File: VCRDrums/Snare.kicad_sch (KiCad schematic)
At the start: 90 parts, among them Q501 BC847, Q502 BC857, Q503 BC847, Q504 BC847, Q505 BC847, Q506 BC857, Q507 BC857, U501 TL074, U502 LM13700, U503 TL074

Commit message: clave in kicad
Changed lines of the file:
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@@
 					(size 1.27 1.27)
 				)
+				(hide yes)
 			)
 		)

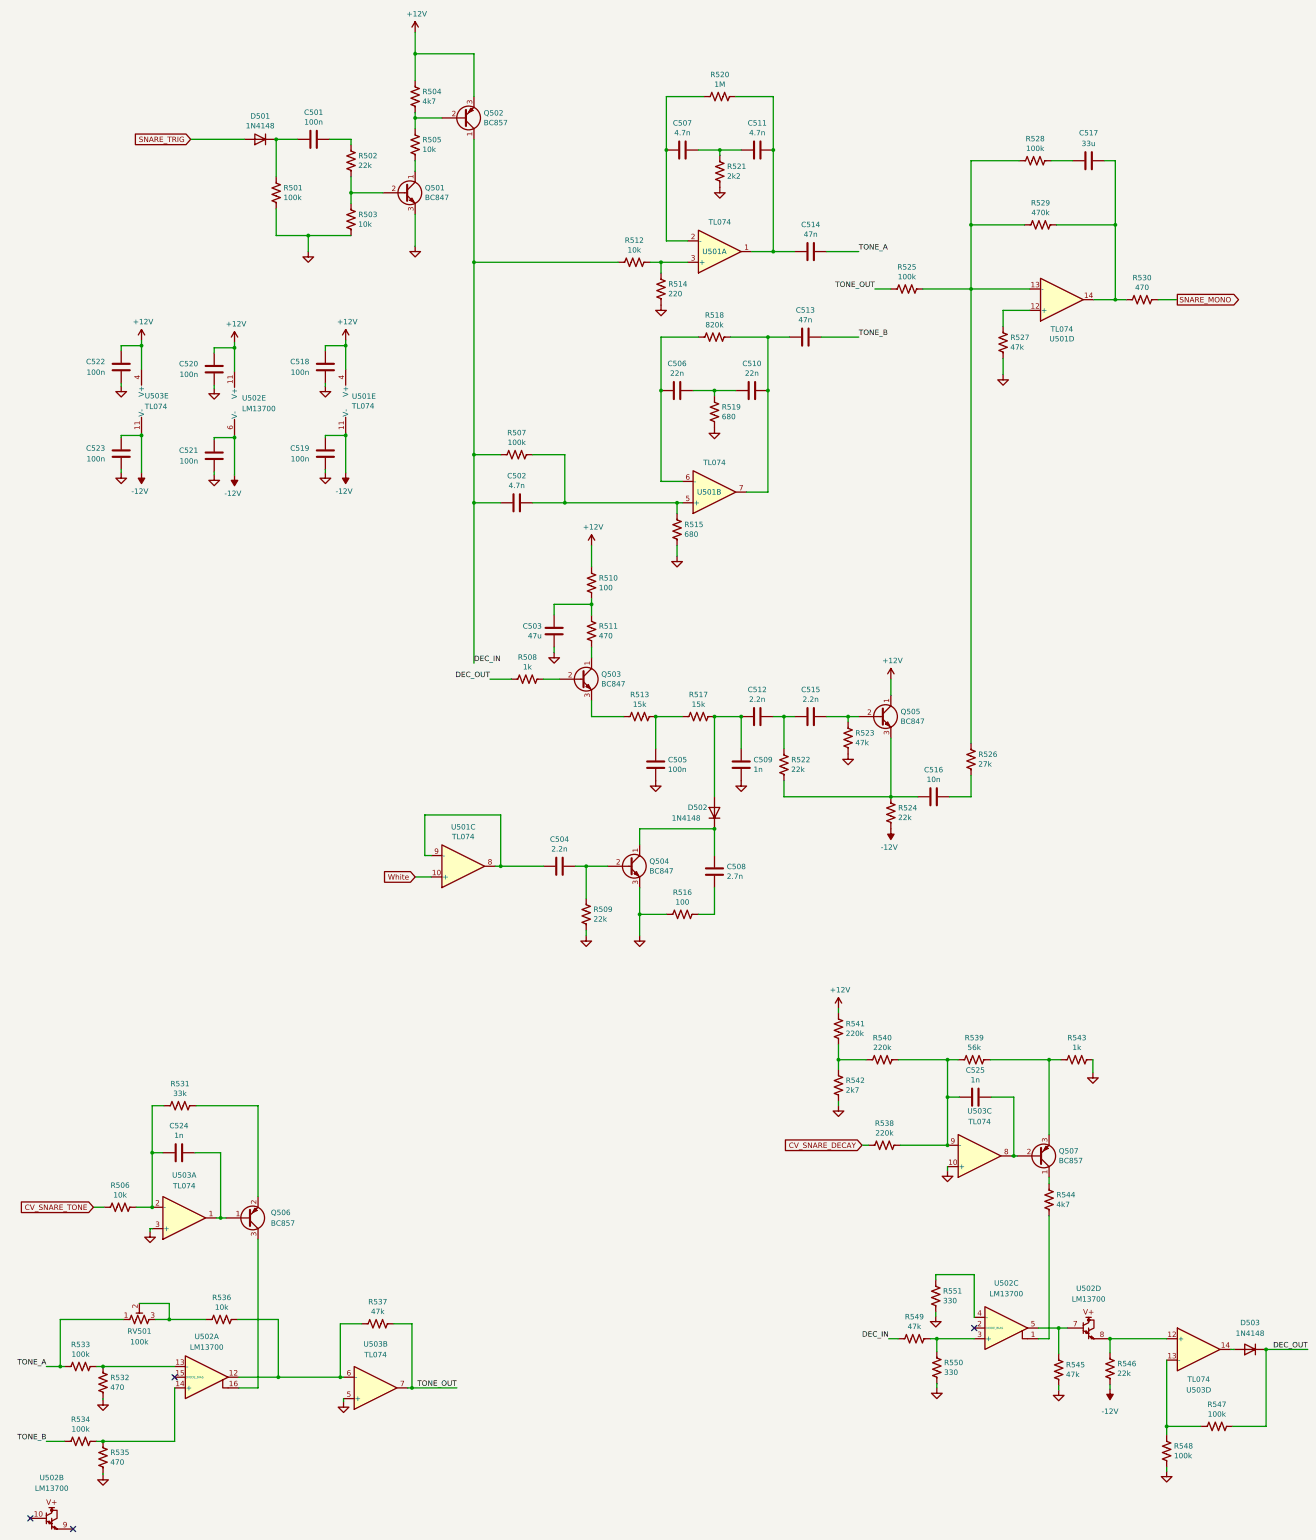
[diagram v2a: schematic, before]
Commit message: mcu skeleton
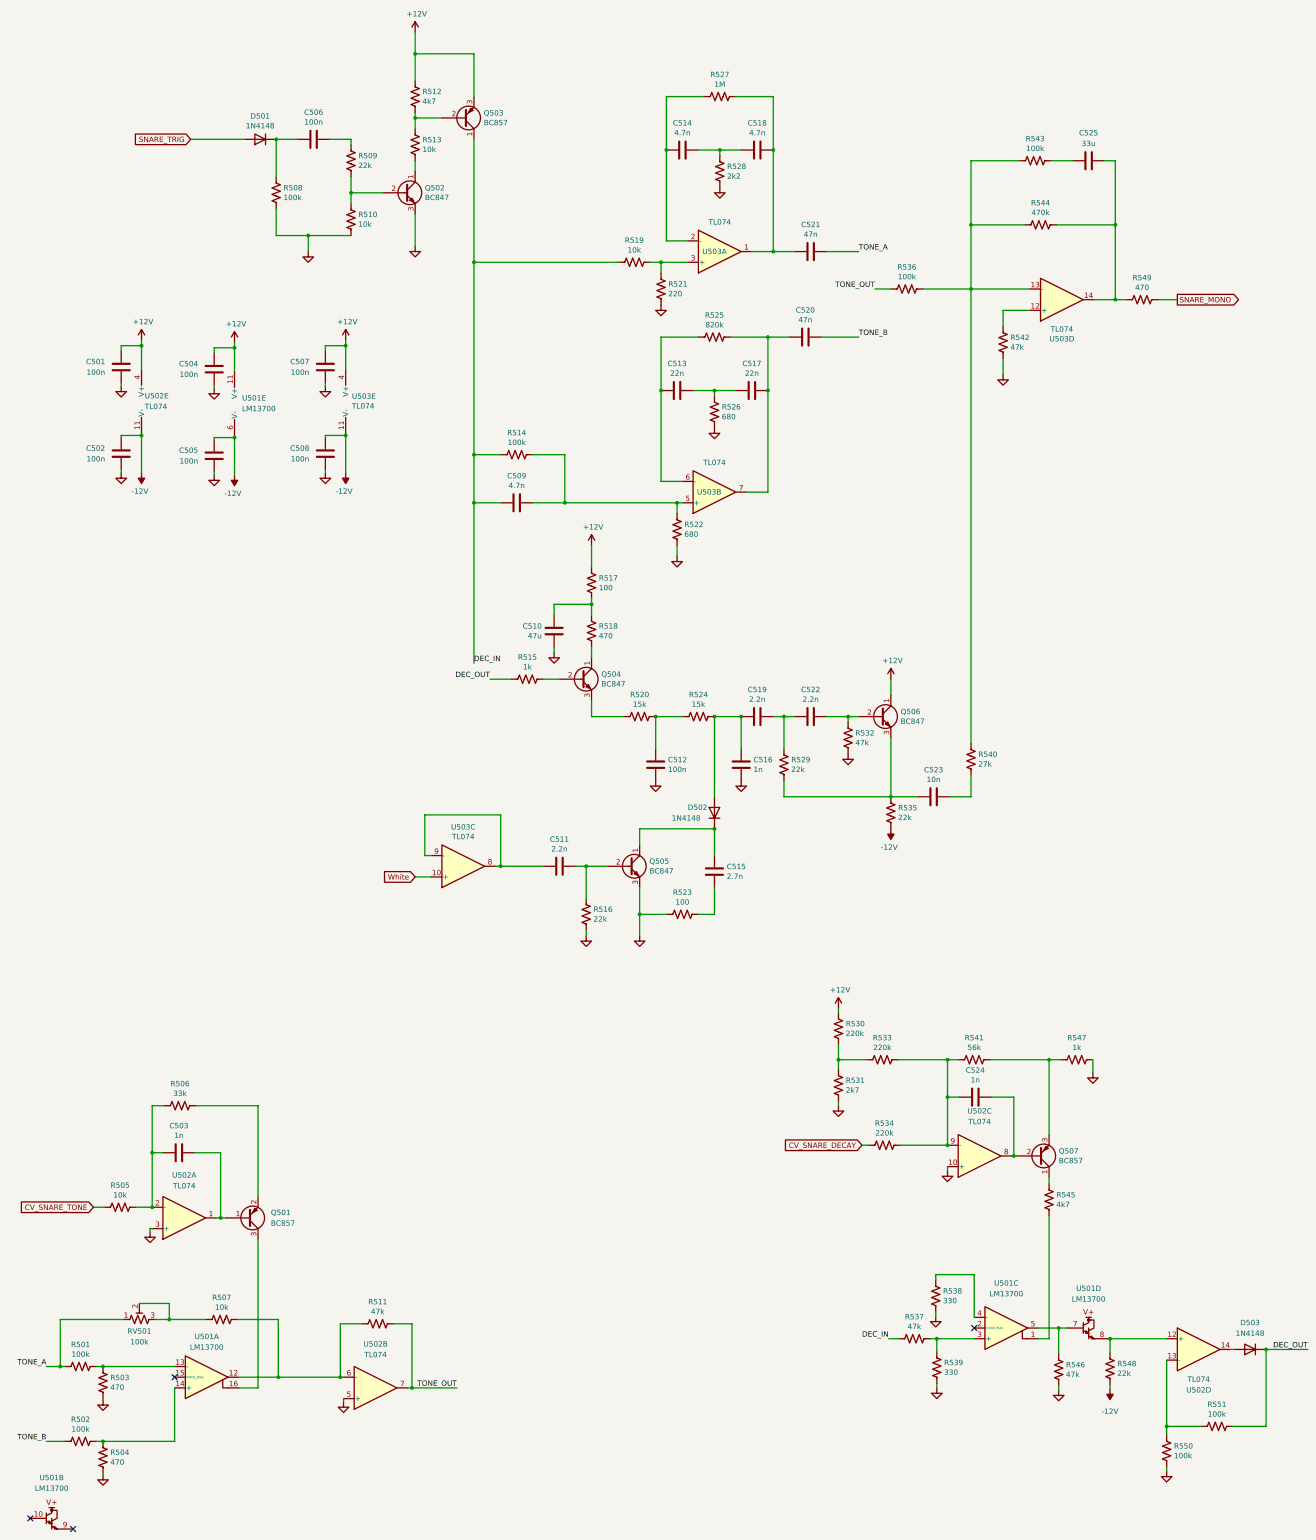
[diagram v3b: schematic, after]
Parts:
- C501: renamed from C522; footprint (none) -> Capacitor_SMD:C_0805_2012Metric
- C502: renamed from C523; footprint (none) -> Capacitor_SMD:C_0805_2012Metric
- C504: renamed from C520; footprint (none) -> Capacitor_SMD:C_0805_2012Metric
- C505: renamed from C521; footprint (none) -> Capacitor_SMD:C_0805_2012Metric
- C507: renamed from C518; footprint (none) -> Capacitor_SMD:C_0805_2012Metric
- C508: renamed from C519; footprint (none) -> Capacitor_SMD:C_0805_2012Metric
- C525: renamed from C517; footprint (none) -> Capacitor_SMD:C_0805_2012Metric
- Q502: renamed from Q501; footprint PCM_4ms_Package_SOT:SOT-23 -> Package_TO_SOT_SMD:SOT-23
- Q503: renamed from Q502; footprint PCM_4ms_Package_SOT:SOT-23 -> Package_TO_SOT_SMD:SOT-23
- Q504: renamed from Q503; footprint PCM_4ms_Package_SOT:SOT-23 -> Package_TO_SOT_SMD:SOT-23
- Q505: renamed from Q504; footprint PCM_4ms_Package_SOT:SOT-23 -> Package_TO_SOT_SMD:SOT-23
- Q506: renamed from Q505; footprint PCM_4ms_Package_SOT:SOT-23 -> Package_TO_SOT_SMD:SOT-23
- Q507: footprint PCM_4ms_Package_SOT:SOT-23 -> Package_TO_SOT_SMD:SOT-23
- R501: renamed from R533; footprint PCM_Resistor_SMD_AKL:R_0805_2012Metric -> Resistor_SMD:R_0805_2012Metric
- R502: renamed from R534; footprint PCM_Resistor_SMD_AKL:R_0805_2012Metric -> Resistor_SMD:R_0805_2012Metric
- R503: renamed from R532; footprint PCM_Resistor_SMD_AKL:R_0805_2012Metric -> Resistor_SMD:R_0805_2012Metric
- R504: renamed from R535; footprint PCM_Resistor_SMD_AKL:R_0805_2012Metric -> Resistor_SMD:R_0805_2012Metric
- R505: renamed from R506; footprint PCM_Resistor_SMD_AKL:R_0805_2012Metric -> Resistor_SMD:R_0805_2012Metric
- R506: renamed from R531; footprint PCM_Resistor_SMD_AKL:R_0805_2012Metric -> Resistor_SMD:R_0805_2012Metric
- R507: renamed from R536; footprint PCM_Resistor_SMD_AKL:R_0805_2012Metric -> Resistor_SMD:R_0805_2012Metric
- R508: renamed from R501; footprint PCM_Resistor_SMD_AKL:R_0805_2012Metric -> Resistor_SMD:R_0805_2012Metric
- R509: renamed from R502; footprint PCM_Resistor_SMD_AKL:R_0805_2012Metric -> Resistor_SMD:R_0805_2012Metric
- R510: renamed from R503; footprint PCM_Resistor_SMD_AKL:R_0805_2012Metric -> Resistor_SMD:R_0805_2012Metric
- R511: renamed from R537; footprint PCM_Resistor_SMD_AKL:R_0805_2012Metric -> Resistor_SMD:R_0805_2012Metric
- R512: renamed from R504; footprint PCM_Resistor_SMD_AKL:R_0805_2012Metric -> Resistor_SMD:R_0805_2012Metric
- R513: renamed from R505; footprint PCM_Resistor_SMD_AKL:R_0805_2012Metric -> Resistor_SMD:R_0805_2012Metric
- R514: renamed from R507; footprint PCM_Resistor_SMD_AKL:R_0805_2012Metric -> Resistor_SMD:R_0805_2012Metric
- R515: renamed from R508; footprint PCM_Resistor_SMD_AKL:R_0805_2012Metric -> Resistor_SMD:R_0805_2012Metric
- R516: renamed from R509; footprint PCM_Resistor_SMD_AKL:R_0805_2012Metric -> Resistor_SMD:R_0805_2012Metric
- R517: renamed from R510; footprint PCM_Resistor_SMD_AKL:R_0805_2012Metric -> Resistor_SMD:R_0805_2012Metric
- R518: renamed from R511; footprint PCM_Resistor_SMD_AKL:R_0805_2012Metric -> Resistor_SMD:R_0805_2012Metric
- R519: renamed from R512; footprint PCM_Resistor_SMD_AKL:R_0805_2012Metric -> Resistor_SMD:R_0805_2012Metric
- R520: renamed from R513; footprint PCM_Resistor_SMD_AKL:R_0805_2012Metric -> Resistor_SMD:R_0805_2012Metric
- R521: renamed from R514; footprint PCM_Resistor_SMD_AKL:R_0805_2012Metric -> Resistor_SMD:R_0805_2012Metric
- R522: renamed from R515; footprint PCM_Resistor_SMD_AKL:R_0805_2012Metric -> Resistor_SMD:R_0805_2012Metric
- R523: renamed from R516; footprint PCM_Resistor_SMD_AKL:R_0805_2012Metric -> Resistor_SMD:R_0805_2012Metric
- R524: renamed from R517; footprint PCM_Resistor_SMD_AKL:R_0805_2012Metric -> Resistor_SMD:R_0805_2012Metric
- R525: renamed from R518; footprint PCM_Resistor_SMD_AKL:R_0805_2012Metric -> Resistor_SMD:R_0805_2012Metric
- R526: renamed from R519; footprint PCM_Resistor_SMD_AKL:R_0805_2012Metric -> Resistor_SMD:R_0805_2012Metric
- R527: renamed from R520; footprint PCM_Resistor_SMD_AKL:R_0805_2012Metric -> Resistor_SMD:R_0805_2012Metric
- R528: renamed from R521; footprint PCM_Resistor_SMD_AKL:R_0805_2012Metric -> Resistor_SMD:R_0805_2012Metric
- R529: renamed from R522; footprint PCM_Resistor_SMD_AKL:R_0805_2012Metric -> Resistor_SMD:R_0805_2012Metric
- R530: renamed from R541; footprint PCM_Resistor_SMD_AKL:R_0805_2012Metric -> Resistor_SMD:R_0805_2012Metric
- R531: renamed from R542; footprint PCM_Resistor_SMD_AKL:R_0805_2012Metric -> Resistor_SMD:R_0805_2012Metric
- R532: renamed from R523; footprint PCM_Resistor_SMD_AKL:R_0805_2012Metric -> Resistor_SMD:R_0805_2012Metric
- R533: renamed from R540; footprint PCM_Resistor_SMD_AKL:R_0805_2012Metric -> Resistor_SMD:R_0805_2012Metric
- R534: renamed from R538; footprint PCM_Resistor_SMD_AKL:R_0805_2012Metric -> Resistor_SMD:R_0805_2012Metric
- R535: renamed from R524; footprint PCM_Resistor_SMD_AKL:R_0805_2012Metric -> Resistor_SMD:R_0805_2012Metric
- R536: renamed from R525; footprint PCM_Resistor_SMD_AKL:R_0805_2012Metric -> Resistor_SMD:R_0805_2012Metric
- R537: renamed from R549; footprint PCM_Resistor_SMD_AKL:R_0805_2012Metric -> Resistor_SMD:R_0805_2012Metric
- R538: renamed from R551; footprint PCM_Resistor_SMD_AKL:R_0805_2012Metric -> Resistor_SMD:R_0805_2012Metric
- R539: renamed from R550; footprint PCM_Resistor_SMD_AKL:R_0805_2012Metric -> Resistor_SMD:R_0805_2012Metric
- R540: renamed from R526; footprint PCM_Resistor_SMD_AKL:R_0805_2012Metric -> Resistor_SMD:R_0805_2012Metric
- R541: renamed from R539; footprint PCM_Resistor_SMD_AKL:R_0805_2012Metric -> Resistor_SMD:R_0805_2012Metric
- R542: renamed from R527; footprint PCM_Resistor_SMD_AKL:R_0805_2012Metric -> Resistor_SMD:R_0805_2012Metric
- R543: renamed from R528; footprint PCM_Resistor_SMD_AKL:R_0805_2012Metric -> Resistor_SMD:R_0805_2012Metric
- R544: renamed from R529; footprint PCM_Resistor_SMD_AKL:R_0805_2012Metric -> Resistor_SMD:R_0805_2012Metric
- R545: renamed from R544; footprint PCM_Resistor_SMD_AKL:R_0805_2012Metric -> Resistor_SMD:R_0805_2012Metric
- R546: renamed from R545; footprint PCM_Resistor_SMD_AKL:R_0805_2012Metric -> Resistor_SMD:R_0805_2012Metric
- R547: renamed from R543; footprint PCM_Resistor_SMD_AKL:R_0805_2012Metric -> Resistor_SMD:R_0805_2012Metric
- R548: renamed from R546; footprint PCM_Resistor_SMD_AKL:R_0805_2012Metric -> Resistor_SMD:R_0805_2012Metric
- R549: renamed from R530; footprint PCM_Resistor_SMD_AKL:R_0805_2012Metric -> Resistor_SMD:R_0805_2012Metric
- R550: renamed from R548; footprint PCM_Resistor_SMD_AKL:R_0805_2012Metric -> Resistor_SMD:R_0805_2012Metric
- R551: renamed from R547; footprint PCM_Resistor_SMD_AKL:R_0805_2012Metric -> Resistor_SMD:R_0805_2012Metric
- RV501: footprint (none) -> Potentiometer_THT:Potentiometer_Bourns_3296W_Vertical
- U501: renamed from U502; footprint (none) -> Package_SO:SOIC-16_3.9x9.9mm_P1.27mm
- U502: renamed from U503; footprint (none) -> Package_SO:SOIC-14_3.9x8.7mm_P1.27mm
- U503: renamed from U501; footprint PCM_Package_SO_AKL:SOIC-14_3.9x8.7mm_P1.27mm -> Package_SO:SOIC-14_3.9x8.7mm_P1.27mm
- renumbered C524 to C503, C501 to C506, C502 to C509, C503 to C510, C504 to C511, C505 to C512, C506 to C513, C507 to C514, C508 to C515, C509 to C516, C510 to C517, C511 to C518, C512 to C519, C513 to C520, C514 to C521, C515 to C522, C516 to C523, C525 to C524, Q506 to Q501

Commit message: compressor schem and schematic
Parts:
- D503: footprint Diode_THT:D_DO-35_SOD27_P7.62mm_Horizontal -> Diode_SMD:D_SOD-123
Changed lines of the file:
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@@
 			)
 		)
-		(property "Footprint" "Diode_THT:D_DO-35_SOD27_P7.62mm_Horizontal"
+		(property "Footprint" "Diode_SMD:D_SOD-123"
 			(at 329.184 347.98 0)
 			(effects
